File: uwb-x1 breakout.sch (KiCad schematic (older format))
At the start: 1 part

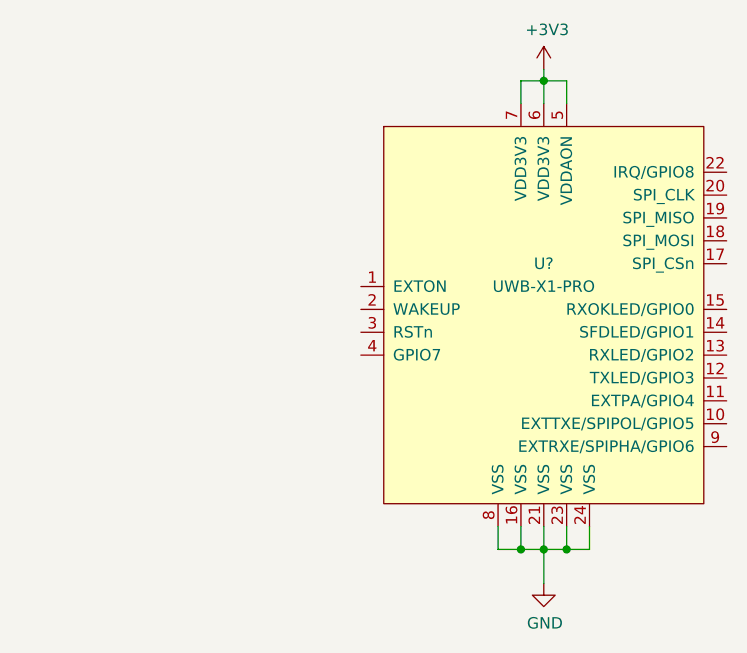
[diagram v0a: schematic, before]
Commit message: Do up schematic for breakout
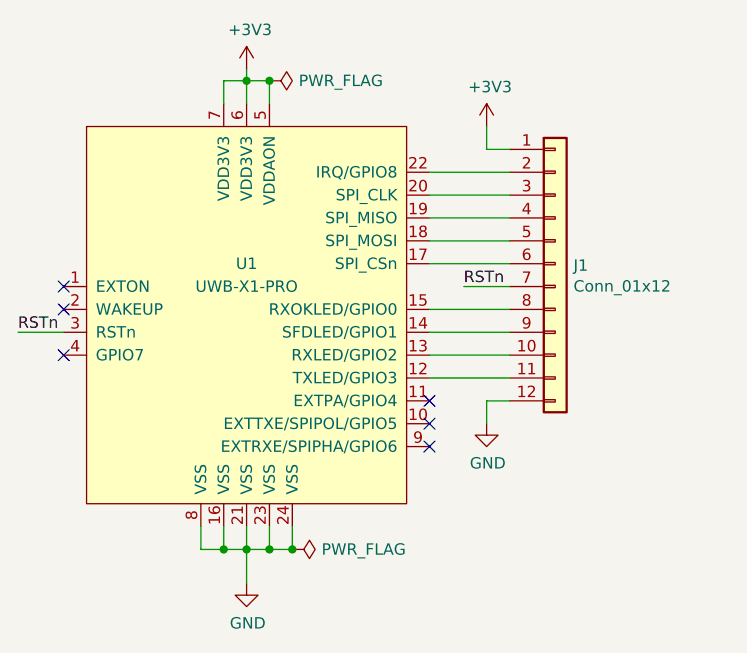
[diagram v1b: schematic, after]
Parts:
- added J1: Conn_01x12, symbol Connector_Generic:Conn_01x12
- gave numbers to parts that had none: 1
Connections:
- net +3V3: now also J1.1 (Pin_1)
- net GND: now also J1.12 (Pin_12)
- net at U1.12 (TXLED/GPIO3): now also J1.11 (Pin_11)
- net at U1.13 (RXLED/GPIO2): now also J1.10 (Pin_10)
- net at U1.14 (SFDLED/GPIO1): now also J1.9 (Pin_9)
- net at U1.15 (RXOKLED/GPIO0): now also J1.8 (Pin_8)
- net at U1.17 (SPI_CSn): now also J1.6 (Pin_6)
- net at U1.18 (SPI_MOSI): now also J1.5 (Pin_5)
- net at U1.19 (SPI_MISO): now also J1.4 (Pin_4)
- net at U1.20 (SPI_CLK): now also J1.3 (Pin_3)
- net at U1.22 (IRQ/GPIO8): now also J1.2 (Pin_2)
- net RSTn: now reaches U1.3 (RSTn)
- net RSTn: now also J1.7 (Pin_7)
- no-connect marks 0 -> 6
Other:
- moved on the sheet: U1
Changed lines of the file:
@@
 $EndDescr
 $Comp
-L UWB-X1:UWB-X1-PRO U?
+L UWB-X1:UWB-X1-PRO U1
 U 1 1 62320BC0
-P 6000 3850
-F 0 "U?" H 6000 4100 50  0000 C CNN
-F 1 "UWB-X1-PRO" H 6000 4000 50  0000 C CNN
-F 2 "" H 5950 3750 50  0001 C CNN
-F 3 "" H 5950 3750 50  0001 C CNN
-	1    6000 3850
+P 4700 3850
+F 0 "U1" H 4700 4100 50  0000 C CNN
+F 1 "UWB-X1-PRO" H 4700 4000 50  0000 C CNN
+F 2 "" H 4650 3750 50  0001 C CNN
+F 3 "" H 4650 3750 50  0001 C CNN
+	1    4700 3850
 	1    0    0    -1
 $EndComp
 Wire Wire Line
-	5900 2900 5900 2800
+	4600 2900 4600 2800
 Wire Wire Line
-	5900 2800 6000 2800
+	4600 2800 4700 2800
 Wire Wire Line
-	6000 2900 6000 2800
+	4700 2900 4700 2800
 Wire Wire Line
-	6100 2900 6100 2800
+	4800 2900 4800 2800
 Wire Wire Line
-	6100 2800 6000 2800
-Connection ~ 6000 2800
+	4800 2800 4700 2800
+Connection ~ 4700 2800
 Wire Wire Line
-	6000 2800 6000 2750
+	4700 2800 4700 2750
 $Comp
-L power:+3V3 #PWR?
+L power:+3V3 #PWR0101
 U 1 1 62322DC0
-P 6000 2750
-F 0 "#PWR?" H 6000 2600 50  0001 C CNN
-F 1 "+3V3" H 6015 2923 50  0000 C CNN
-F 2 "" H 6000 2750 50  0001 C CNN
-F 3 "" H 6000 2750 50  0001 C CNN
-	1    6000 2750
+P 4700 2750
+F 0 "#PWR0101" H 4700 2600 50  0001 C CNN
+F 1 "+3V3" H 4715 2923 50  0000 C CNN
+F 2 "" H 4700 2750 50  0001 C CNN
+F 3 "" H 4700 2750 50  0001 C CNN
+	1    4700 2750
 	1    0    0    -1
 $EndComp
 $Comp
-L power:GND #PWR?
+L power:GND #PWR0102
 U 1 1 623241FD
-P 6000 5000
-F 0 "#PWR?" H 6000 4750 50  0001 C CNN
-F 1 "GND" H 6005 4827 50  0000 C CNN
-F 2 "" H 6000 5000 50  0001 C CNN
-F 3 "" H 6000 5000 50  0001 C CNN
-	1    6000 5000
+P 4700 5000
+F 0 "#PWR0102" H 4700 4750 50  0001 C CNN
+F 1 "GND" H 4705 4827 50  0000 C CNN
+F 2 "" H 4700 5000 50  0001 C CNN
+F 3 "" H 4700 5000 50  0001 C CNN
+	1    4700 5000
 	1    0    0    -1
 $EndComp
 Wire Wire Line
-	5800 4750 5800 4850
+	4500 4750 4500 4850
 Wire Wire Line
-	5800 4850 5900 4850
+	4500 4850 4600 4850
 Wire Wire Line
-	6200 4850 6200 4750
+	4900 4850 4900 4750
 Wire Wire Line
-	5900 4750 5900 4850
-Connection ~ 5900 4850
+	4600 4750 4600 4850
+Connection ~ 4600 4850
 Wire Wire Line
-	5900 4850 6000 4850
+	4600 4850 4700 4850
 Wire Wire Line
-	6100 4750 6100 4850
-Connection ~ 6100 4850
+	4800 4750 4800 4850
+Connection ~ 4800 4850
 Wire Wire Line
-	6100 4850 6200 4850
+	4800 4850 4900 4850
 Wire Wire Line
-	6000 4750 6000 4850
-Connection ~ 6000 4850
+	4700 4750 4700 4850
+Connection ~ 4700 4850
 Wire Wire Line
-	6000 4850 6100 4850
+	4700 4850 4800 4850
 Wire Wire Line
-	6000 4850 6000 5000
+	4700 4850 4700 5000
+NoConn ~ 3900 3700
+NoConn ~ 3900 3800
+NoConn ~ 3900 4000
+NoConn ~ 5500 4200
+NoConn ~ 5500 4300
+NoConn ~ 5500 4400
+Wire Wire Line
+	5500 3600 5850 3600
+Wire Wire Line
+	5500 3500 5850 3500
+Wire Wire Line
+	5500 3400 5850 3400
+Wire Wire Line
+	5500 3300 5850 3300
+Wire Wire Line
+	5500 3200 5850 3200
+Wire Wire Line
+	5850 3100 5750 3100
+Wire Wire Line
+	5750 3100 5750 3000
+$Comp
+L power:+3V3 #PWR0103
+U 1 1 623327F0
+P 5750 3000
+F 0 "#PWR0103" H 5750 2850 50  0001 C CNN
+F 1 "+3V3" H 5765 3173 50  0000 C CNN
+F 2 "" H 5750 3000 50  0001 C CNN
+F 3 "" H 5750 3000 50  0001 C CNN
+	1    5750 3000
+	1    0    0    -1
+$EndComp
+$Comp
+L Connector_Generic:Conn_01x12 J1
+U 1 1 62340FC2
+P 6050 3600
+F 0 "J1" H 6130 3592 50  0000 L CNN
+F 1 "Conn_01x12" H 6130 3501 50  0000 L CNN
+F 2 "" H 6050 3600 50  0001 C CNN
+F 3 "~" H 6050 3600 50  0001 C CNN
+	1    6050 3600
+	1    0    0    -1
+$EndComp
+Wire Wire Line
+	5500 4100 5850 4100
+Wire Wire Line
+	5500 4000 5850 4000
+Wire Wire Line
+	5500 3900 5850 3900
+Wire Wire Line
+	5500 3800 5850 3800
+Wire Wire Line
+	3900 3900 3700 3900
+Text Label 3700 3900 0    50   ~ 0
+RSTn
+Wire Wire Line
+	5850 3700 5650 3700
+Text Label 5650 3700 0    50   ~ 0
+RSTn
+$Comp
+L power:GND #PWR0104
+U 1 1 623332F8
+P 5750 4300
+F 0 "#PWR0104" H 5750 4050 50  0001 C CNN
+F 1 "GND" H 5755 4127 50  0000 C CNN
+F 2 "" H 5750 4300 50  0001 C CNN
+F 3 "" H 5750 4300 50  0001 C CNN
+	1    5750 4300
+	1    0    0    -1
+$EndComp
+Wire Wire Line
+	5750 4200 5750 4300
+Wire Wire Line
+	5750 4200 5850 4200
+$Comp
+L power:PWR_FLAG #FLG0101
+U 1 1 6234AF73
+P 4800 2800
+F 0 "#FLG0101" H 4800 2875 50  0001 C CNN
+F 1 "PWR_FLAG" V 4800 2928 50  0000 L CNN
+F 2 "" H 4800 2800 50  0001 C CNN
+F 3 "~" H 4800 2800 50  0001 C CNN
+	1    4800 2800
+	0    1    1    0
+$EndComp
+Connection ~ 4800 2800
+Connection ~ 4900 4850
+$Comp
+L power:PWR_FLAG #FLG0102
+U 1 1 6234C5C4
+P 4900 4850
+F 0 "#FLG0102" H 4900 4925 50  0001 C CNN
+F 1 "PWR_FLAG" V 4900 4978 50  0000 L CNN
+F 2 "" H 4900 4850 50  0001 C CNN
+F 3 "~" H 4900 4850 50  0001 C CNN
+	1    4900 4850
+	0    1    1    0
+$EndComp
 $EndSCHEMATC

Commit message: Create PCB schema
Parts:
- J1: footprint (none) -> Connector_PinHeader_2.54mm:PinHeader_1x12_P2.54mm_Vertical
- U1: footprint (none) -> UWB-X1:UWB-X1-CA
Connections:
- net +3V3: now also J1.11 (Pin_11); no longer J1.1 (Pin_1)
- net RSTn: now also J1.10 (Pin_10); no longer J1.7 (Pin_7)
- net at U1.12 (TXLED/GPIO3): now also J1.9 (Pin_9); no longer J1.11 (Pin_11)
- net at U1.13 (RXLED/GPIO2): now also J1.8 (Pin_8); no longer J1.10 (Pin_10)
- net at U1.14 (SFDLED/GPIO1): now also J1.7 (Pin_7); no longer J1.9 (Pin_9)
- net at U1.15 (RXOKLED/GPIO0): now also J1.6 (Pin_6); no longer J1.8 (Pin_8)
- net at U1.17 (SPI_CSn): now also J1.5 (Pin_5); no longer J1.6 (Pin_6)
- net at U1.18 (SPI_MOSI): now also J1.4 (Pin_4); no longer J1.5 (Pin_5)
- net at U1.19 (SPI_MISO): now also J1.3 (Pin_3); no longer J1.4 (Pin_4)
- net at U1.20 (SPI_CLK): now also J1.2 (Pin_2); no longer J1.3 (Pin_3)
- net at U1.22 (IRQ/GPIO8): now also J1.1 (Pin_1); no longer J1.2 (Pin_2)
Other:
- moved on the sheet: J1
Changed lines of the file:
@@
 Comment4 ""
 $EndDescr
-$Comp
-L UWB-X1:UWB-X1-PRO U1
-U 1 1 62320BC0
-P 4700 3850
-F 0 "U1" H 4700 4100 50  0000 C CNN
-F 1 "UWB-X1-PRO" H 4700 4000 50  0000 C CNN
-F 2 "" H 4650 3750 50  0001 C CNN
-F 3 "" H 4650 3750 50  0001 C CNN
-	1    4700 3850
-	1    0    0    -1
-$EndComp
 Wire Wire Line
 	4600 2900 4600 2800
@@
 NoConn ~ 5500 4400
 Wire Wire Line
-	5500 3600 5850 3600
-Wire Wire Line
-	5500 3500 5850 3500
-Wire Wire Line
-	5500 3400 5850 3400
-Wire Wire Line
-	5500 3300 5850 3300
-Wire Wire Line
-	5500 3200 5850 3200
-Wire Wire Line
-	5850 3100 5750 3100
-Wire Wire Line
-	5750 3100 5750 3000
+	3900 3900 3700 3900
+Text Label 3700 3900 0    50   ~ 0
+RSTn
 $Comp
-L power:+3V3 #PWR0103
-U 1 1 623327F0
-P 5750 3000
-F 0 "#PWR0103" H 5750 2850 50  0001 C CNN
-F 1 "+3V3" H 5765 3173 50  0000 C CNN
-F 2 "" H 5750 3000 50  0001 C CNN
-F 3 "" H 5750 3000 50  0001 C CNN
-	1    5750 3000
+L UWB-X1:UWB-X1-PRO U1
+U 1 1 62320BC0
+P 4700 3850
+F 0 "U1" H 4700 4100 50  0000 C CNN
+F 1 "UWB-X1-PRO" H 4700 4000 50  0000 C CNN
+F 2 "UWB-X1:UWB-X1-CA" H 4650 3750 50  0001 C CNN
+F 3 "" H 4650 3750 50  0001 C CNN
+	1    4700 3850
 	1    0    0    -1
 $EndComp
-$Comp
-L Connector_Generic:Conn_01x12 J1
-U 1 1 62340FC2
-P 6050 3600
-F 0 "J1" H 6130 3592 50  0000 L CNN
-F 1 "Conn_01x12" H 6130 3501 50  0000 L CNN
-F 2 "" H 6050 3600 50  0001 C CNN
-F 3 "~" H 6050 3600 50  0001 C CNN
-	1    6050 3600
-	1    0    0    -1
-$EndComp
+Wire Wire Line
+	5500 3200 5800 3200
 Wire Wire Line
 	5500 4100 5850 4100
@@
 Wire Wire Line
 	5500 3800 5850 3800
-Wire Wire Line
-	3900 3900 3700 3900
-Text Label 3700 3900 0    50   ~ 0
-RSTn
-Wire Wire Line
-	5850 3700 5650 3700
-Text Label 5650 3700 0    50   ~ 0
-RSTn
-$Comp
-L power:GND #PWR0104
-U 1 1 623332F8
-P 5750 4300
-F 0 "#PWR0104" H 5750 4050 50  0001 C CNN
-F 1 "GND" H 5755 4127 50  0000 C CNN
-F 2 "" H 5750 4300 50  0001 C CNN
-F 3 "" H 5750 4300 50  0001 C CNN
-	1    5750 4300
-	1    0    0    -1
-$EndComp
-Wire Wire Line
-	5750 4200 5750 4300
-Wire Wire Line
-	5750 4200 5850 4200
 $Comp
 L power:PWR_FLAG #FLG0101
@@
 $EndComp
 Connection ~ 4800 2800
-Connection ~ 4900 4850
 $Comp
 L power:PWR_FLAG #FLG0102
@@
 	0    1    1    0
 $EndComp
+Connection ~ 4900 4850
+$Comp
+L Connector_Generic:Conn_01x12 J1
+U 1 1 62340FC2
+P 6050 3800
+F 0 "J1" H 6130 3792 50  0000 L CNN
+F 1 "Conn_01x12" H 6130 3701 50  0000 L CNN
+F 2 "Connector_PinHeader_2.54mm:PinHeader_1x12_P2.54mm_Vertical" H 6050 3800 50  0001 C CNN
+F 3 "~" H 6050 3800 50  0001 C CNN
+	1    6050 3800
+	1    0    0    -1
+$EndComp
+Wire Wire Line
+	5850 4200 5650 4200
+Text Label 5650 4200 0    50   ~ 0
+RSTn
+$Comp
+L power:GND #PWR0104
+U 1 1 623332F8
+P 5800 4500
+F 0 "#PWR0104" H 5800 4250 50  0001 C CNN
+F 1 "GND" H 5805 4327 50  0000 C CNN
+F 2 "" H 5800 4500 50  0001 C CNN
+F 3 "" H 5800 4500 50  0001 C CNN
+	1    5800 4500
+	1    0    0    -1
+$EndComp
+Wire Wire Line
+	5850 4400 5800 4400
+Wire Wire Line
+	5800 4400 5800 4500
+$Comp
+L power:+3V3 #PWR0103
+U 1 1 623327F0
+P 5600 4500
+F 0 "#PWR0103" H 5600 4350 50  0001 C CNN
+F 1 "+3V3" H 5615 4673 50  0000 C CNN
+F 2 "" H 5600 4500 50  0001 C CNN
+F 3 "" H 5600 4500 50  0001 C CNN
+	1    5600 4500
+	1    0    0    1
+$EndComp
+Wire Wire Line
+	5600 4500 5600 4300
+Wire Wire Line
+	5600 4300 5850 4300
+Wire Wire Line
+	5600 3600 5600 3700
+Wire Wire Line
+	5600 3700 5850 3700
+Wire Wire Line
+	5500 3600 5600 3600
+Wire Wire Line
+	5500 3500 5650 3500
+Wire Wire Line
+	5650 3500 5650 3600
+Wire Wire Line
+	5650 3600 5850 3600
+Wire Wire Line
+	5500 3400 5700 3400
+Wire Wire Line
+	5700 3400 5700 3500
+Wire Wire Line
+	5700 3500 5850 3500
+Wire Wire Line
+	5500 3300 5750 3300
+Wire Wire Line
+	5750 3300 5750 3400
+Wire Wire Line
+	5750 3400 5850 3400
+Wire Wire Line
+	5800 3300 5850 3300
+Wire Wire Line
+	5800 3200 5800 3300
 $EndSCHEMATC
